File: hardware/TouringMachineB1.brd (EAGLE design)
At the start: 30.2 x 106.5 mm, 64 parts, among them IC1 78L05F, J1 PJ301_THONKICONN6, J2 PJ301_THONKICONN6, J3 PJ301_THONKICONN6, J4 PJ301_THONKICONN6, J5 POWER_SIMPLE10-OTHERSIDE, U1 MCP6002_, U2 TL072_SMD

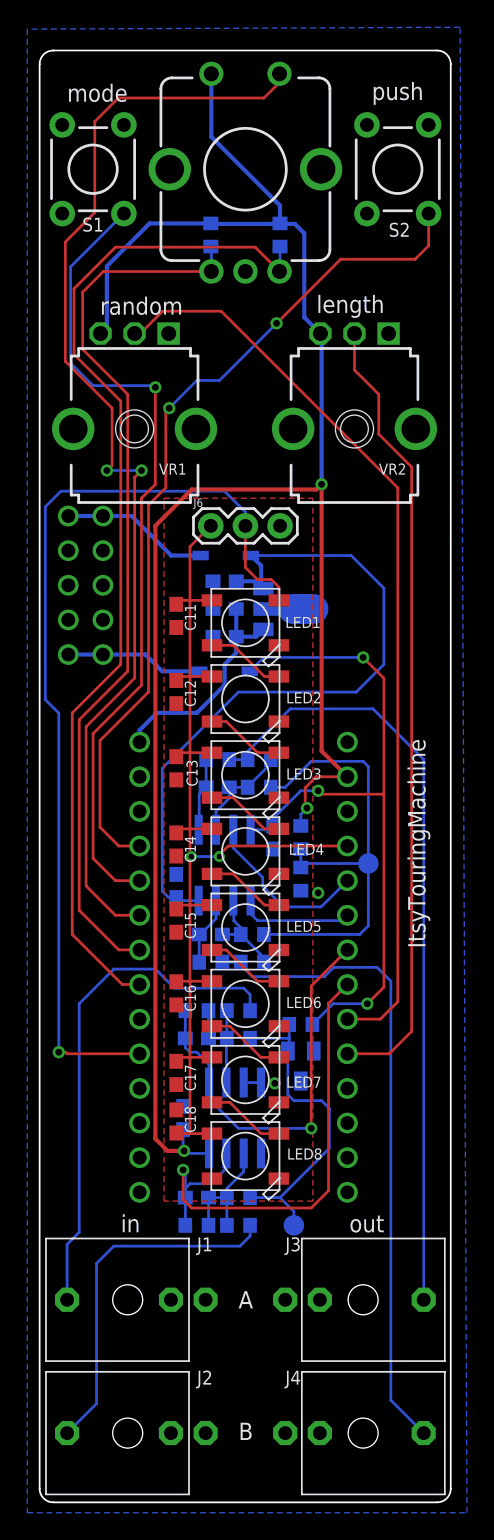
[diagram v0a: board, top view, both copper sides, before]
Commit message: cleaned up UI after knobtesterA results
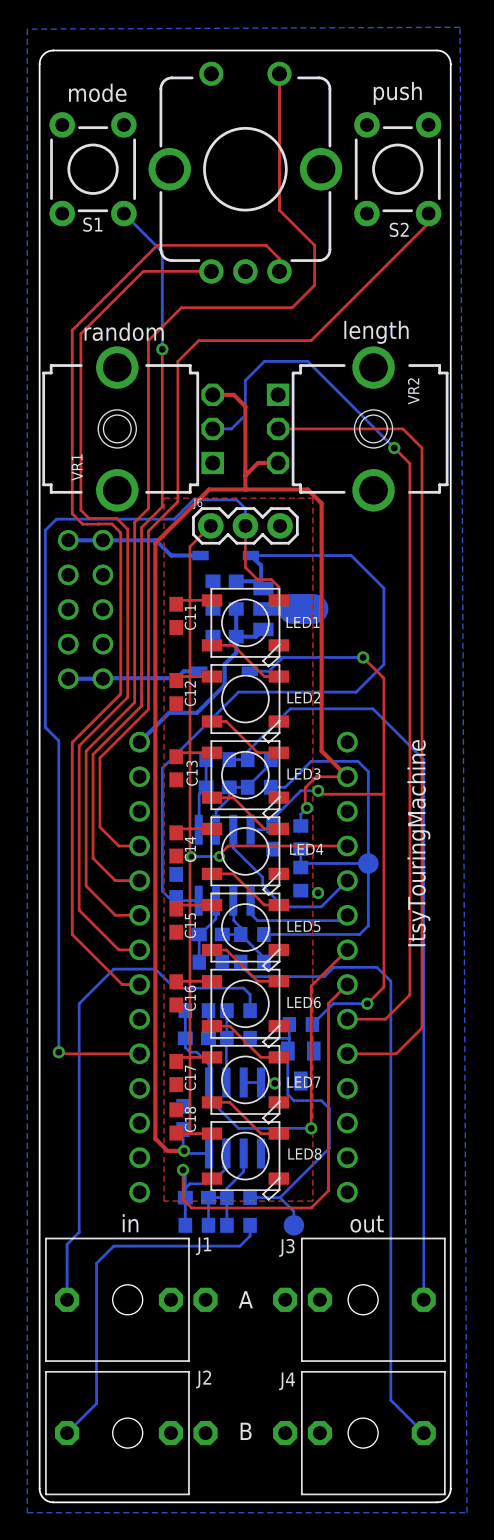
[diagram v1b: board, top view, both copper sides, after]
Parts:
- removed R16, R17: 10k, resistor:R0603
- moved J5 1.78 mm to (3.52, 65.5)
- moved VR2 1.40 mm to (24.6, 78.7), turned to 270 degrees
- moved VR1 1.27 mm to (5.84, 78.7), turned to 90 degrees
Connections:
- net +3V3: no longer R16.1, R17.2, U$1.SW1
- net ENCA: no longer R16.2
- net ENCB: no longer R17.1
- net GND: now also U$1.SW1
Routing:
- net +3V3: track 147.0 -> 103.5 mm, vias 3 -> 2
- net ENCSW: track 83.0 -> 77.2 mm, vias 2 -> 0
- net SW1: track 60.1 -> 54.7 mm
- net ENCA: track 65.7 -> 63.5 mm
- net KNOB1: track 67.3 -> 65.4 mm, vias 0 -> 1
- net KNOB2: track 58.3 -> 59.9 mm
- net ENCB: track 75.6 -> 74.1 mm
- net NEODAT: track 70.3 -> 68.9 mm
- net N$8: track 10.9 -> 10.2 mm
- net SW2: track 62.6 -> 63.3 mm, vias 2 -> 0
- net +5V: track 16.6 -> 16.1 mm
